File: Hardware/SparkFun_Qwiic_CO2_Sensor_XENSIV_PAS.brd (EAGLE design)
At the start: 25.4 x 40.6 mm, 72 parts, among them J1 QWIIC_RA, J2 QWIIC_RA, U1 PASCO2V01BUMA1, U2 LMR62421

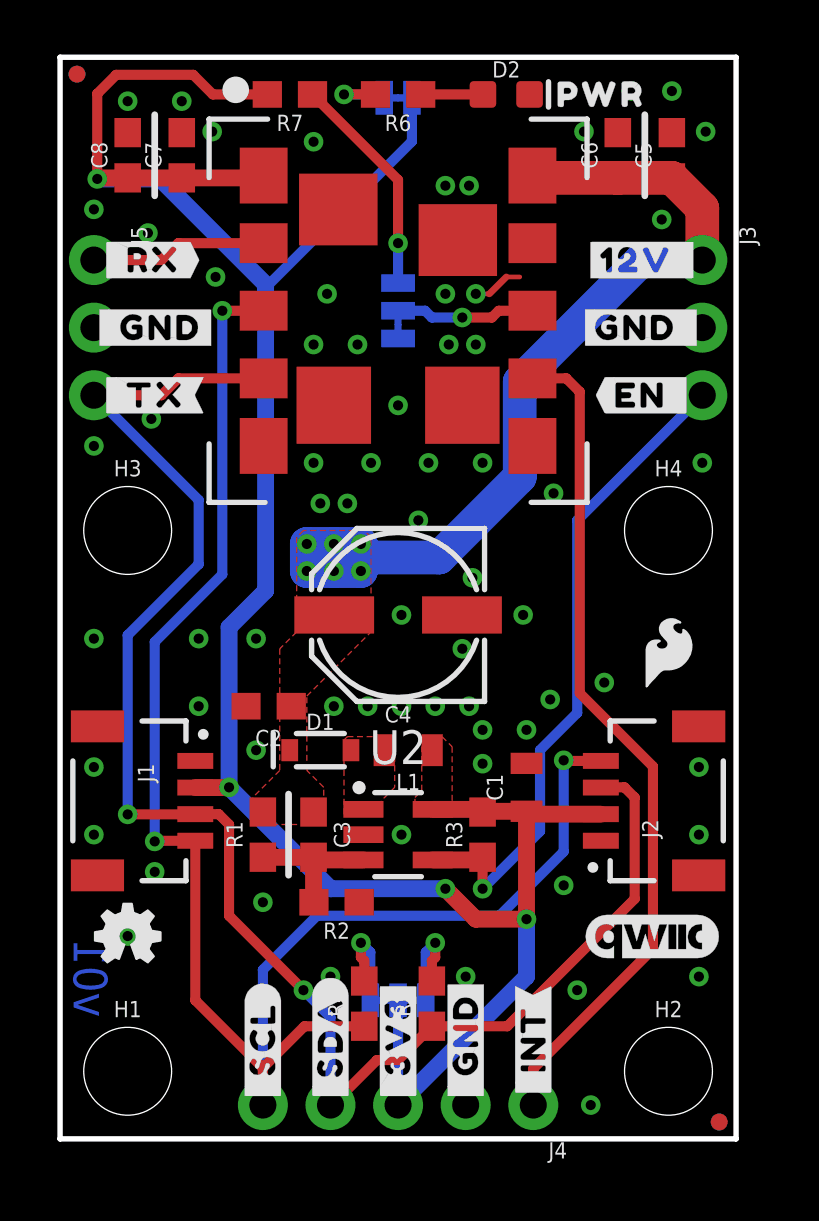
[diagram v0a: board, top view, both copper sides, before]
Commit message: Post design review changes and gerbers.
Add tDocu for the can and put squares for PnP.
Move EN to bottom row.
Rearrange I2C PTHs on bottom row to align with prior art.
Add PWM/PWM_DIS breakout.
Change silk on 12V to 12VIN.
Shift vertical PTHs down 0.05 to line up with perfboard holes.
Create gerbers.
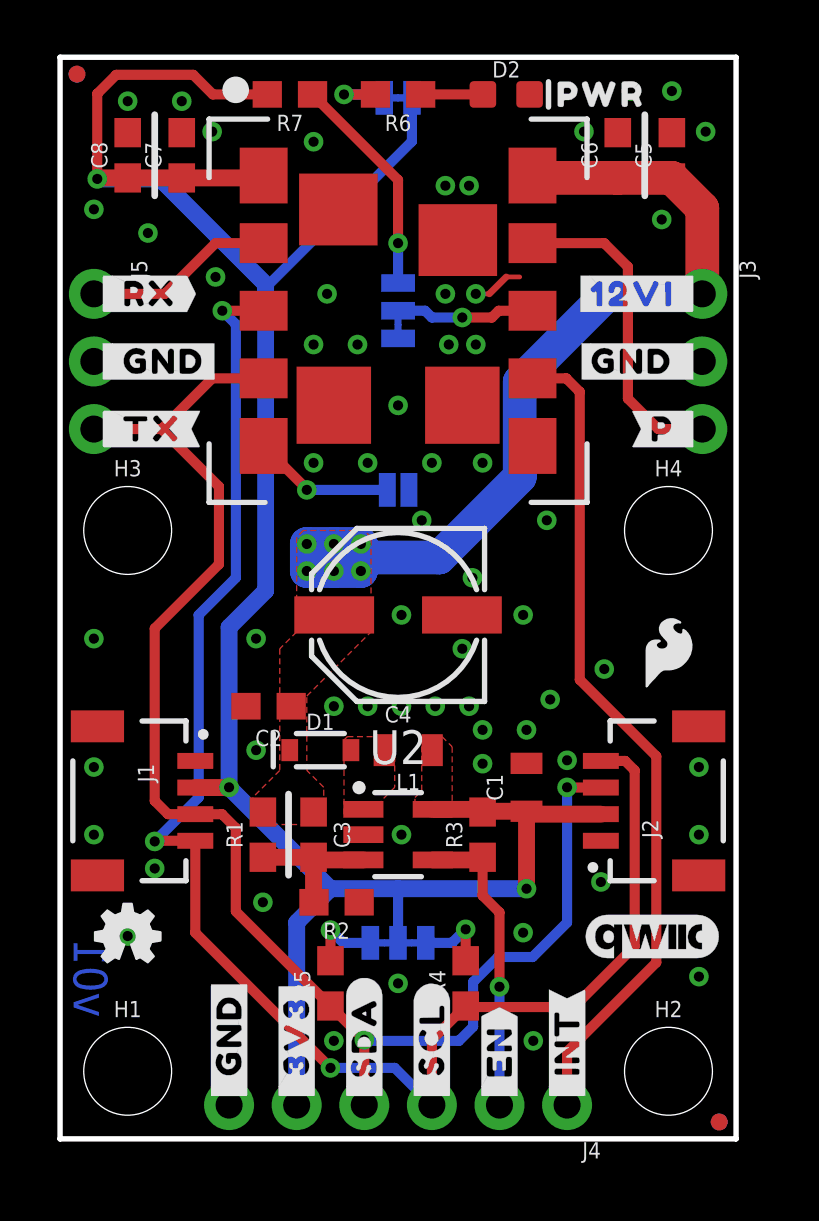
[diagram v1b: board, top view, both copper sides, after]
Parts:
- added PWM: JUMPER-SMT_2_NO_SILK, SparkFun-Jumpers:SMT-JUMPER_2_NO_SILK
- added U$33: (no value), output:#12VI_#0
- added U$34: (no value), output:#_PWM#0
- added U$35: (no value), output:#_SDA#0
- added U$36: (no value), output:#_SCL#0
- J4: device SparkFun-Connectors:1X05_NO_SILK -> SparkFun-Connectors:1X06_NO_SILK
- U$11: device output:#_12V#0 -> output:#_3V3#0
- U$16: device output:#_SDA#0 -> output:#PWM#0
- U$17: device output:#_SCL#0 -> output:#P_#0
- U$2: device output:#12V_#0 -> output:#_12VIN#0
- U$20: device output:#_SDA#TX#0 -> output:#_SDA#0
- U$3: device output:#EN_#0 -> output:#_EN#0
- moved U$11 33.5 mm to (8.89, 1.27), turned to 90 degrees
- moved U$17 30.3 mm to (24.1, 26.7), flipped to the top, turned to 0 degrees
- moved U$3 27.7 mm to (16.5, 1.27), turned to 90 degrees
- moved U$10 26.9 mm to (16.5, 1.27), turned to 90 degrees
- moved U$16 23.3 mm to (13.5, 24.4), flipped to the bottom, turned to 0 degrees
- moved U$14 8.89 mm to (6.35, 1.27)
- moved U$18 8.89 mm to (6.35, 1.27)
- moved U$15 6.35 mm to (14.0, 1.27)
- moved R4 3.89 mm to (15.2, 5.84)
- moved R5 3.89 mm to (10.2, 5.84)
- moved U$19 3.81 mm to (8.89, 1.27)
- moved I2C 2.16 mm to (12.7, 7.37), turned to 180 degrees
- moved U$27 2.16 mm to (12.7, 9.02)
- moved U$28 2.05 mm to (13.6, 39.1)
- moved U$12 1.28 mm to (1.27, 31.8)
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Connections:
- new net N$9: PWM.2, U1.5
- new net PWM_OUT: J3.3, U1.9
- net 3.3V: now also J4.5; no longer J4.3
- net EN: now also J4.2; no longer J3.3
- net GND: now also J4.6, PWM.1; no longer J4.2
- net SCL: now also J4.3; no longer J4.5
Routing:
- net EN: track 25.1 -> 11.5 mm
- net PWM_OUT: track 0.00 -> 12.2 mm
- net SDA/TX: track 61.1 -> 55.7 mm
- net N$9: track 0.00 -> 5.35 mm, vias 0 -> 1
- net 3.3V: track 91.2 -> 87.4 mm, vias 4 -> 3
- net SCL: track 62.6 -> 59.1 mm
- net N$1: track 3.79 -> 2.85 mm
- net N$3: track 3.79 -> 2.89 mm
- net 12V: track 35.7 -> 36.5 mm
- net RX: track 6.64 -> 7.17 mm
- net GND: vias 66 -> 60

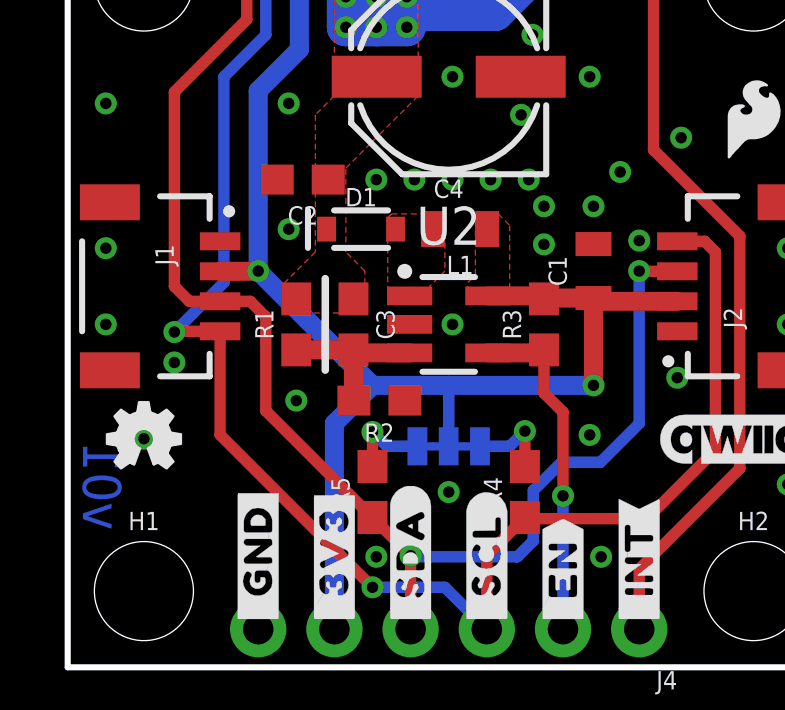
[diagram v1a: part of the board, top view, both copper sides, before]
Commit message: Update for v10.
Schematic - Make version v10.
Board - Make version v10. Change size of Silk title text.
Production - Removed individual board gerbers, add panel gerbers.
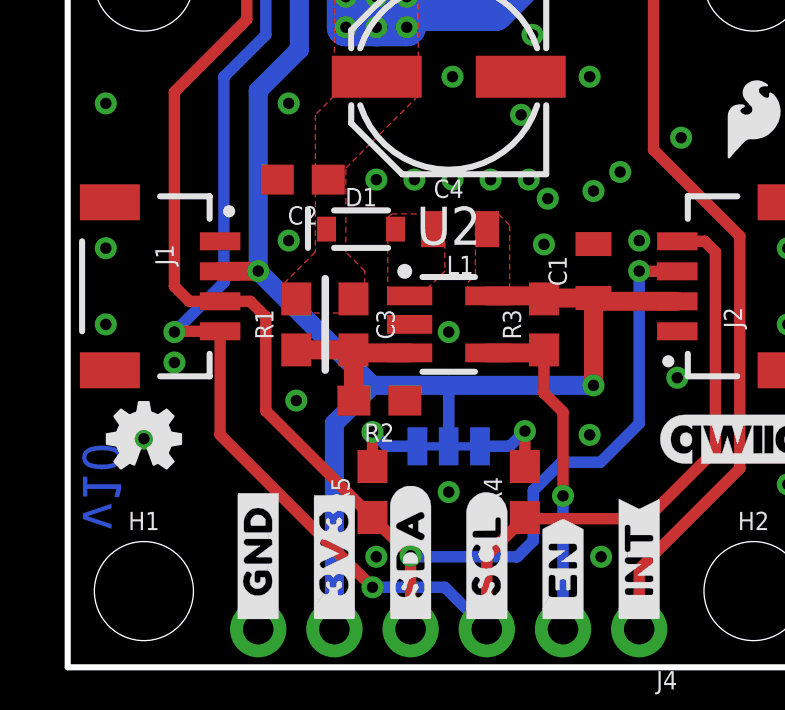
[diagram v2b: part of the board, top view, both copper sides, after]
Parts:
- removed U$23: (no value), output:CO2_SENSOR_#_PASCO2V010
- added U$37: (no value), output:PHOTOACOUSTIC0
- added U$38: (no value), output:SPECTROSCOPY0
- added U$39: (no value), output:PASCO2V010
- U$25: device output:PHOTOACOUSTIC_SPECTROSCOPY0 -> output:CO2_SENSOR0
- moved U$25 0.51 mm to (12.7, 11.9)
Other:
- board text added: "v10"
- board text removed: "v01"
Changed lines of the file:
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@@
 <drawing>
 <settings>
-<setting alwaysvectorfont="yes"/>
+<setting alwaysvectorfont="no"/>
 <setting verticaltext="up"/>
 </settings>
@@
 <layer number="27" name="tValues" color="7" fill="1" visible="no" active="yes"/>
 <layer number="28" name="bValues" color="7" fill="1" visible="no" active="yes"/>
-<layer number="29" name="tStop" color="7" fill="3" visible="yes" active="yes"/>
-<layer number="30" name="bStop" color="7" fill="6" visible="yes" active="yes"/>
-<layer number="31" name="tCream" color="7" fill="4" visible="yes" active="yes"/>
+<layer number="29" name="tStop" color="7" fill="3" visible="no" active="yes"/>
+<layer number="30" name="bStop" color="7" fill="6" visible="no" active="yes"/>
+<layer number="31" name="tCream" color="7" fill="4" visible="no" active="yes"/>
 <layer number="32" name="bCream" color="7" fill="5" visible="no" active="yes"/>
 <layer number="33" name="tFinish" color="6" fill="3" visible="no" active="yes"/>
@@
 <wire x1="8.5852" y1="12.954" x2="8.5852" y2="9.906" width="0.254" layer="21"/>
 <wire x1="3.556" y1="38.481" x2="3.556" y2="35.433" width="0.254" layer="21"/>
-<text x="0.508" y="4.572" size="1.27" layer="16" font="vector" ratio="15" rot="MR90">v01</text>
+<text x="0.508" y="4.572" size="1.27" layer="16" font="vector" ratio="15" rot="MR90">v10</text>
 <dimension x1="0" y1="0" x2="12.7" y2="31.115" x3="6.35" y3="-10.287" textsize="1.27" textratio="15" layer="47" dtype="horizontal" unit="inch"/>
 <dimension x1="0" y1="0" x2="22.86" y2="2.54" x3="11.43" y3="-13.081" textsize="1.27" textratio="15" layer="47" dtype="horizontal" unit="inch"/>
@@
 <element name="FRAME1" library="SparkFun-Aesthetics" package="CREATIVE_COMMONS" value="FRAME-LETTER" x="51.943" y="-9.398" smashed="yes">
 <attribute name="DESIGNER" value="Alex Brudner" x="51.943" y="-9.398" size="1.778" layer="27" display="off"/>
-<attribute name="REV" value="v01" x="51.943" y="-9.398" size="1.778" layer="27" display="off"/>
+<attribute name="REV" value="v10" x="51.943" y="-9.398" size="1.778" layer="27" display="off"/>
 </element>
 <element name="U1" library="xensiv_pas" package="LG-MLGA-14-1_Z8B00206105" value="PASCO2V01BUMA1" x="12.7" y="31.115" smashed="yes" rot="R270">
@@
 <element name="U2" library="xensiv_pas" package="SOT95P280X145-5M" package3d_urn="urn:adsk.eagle:package:40937508/1" value="LMR62421" x="12.7" y="11.43" smashed="yes">
 <attribute name="NAME" x="12.7" y="14.0836" size="1.27" layer="25" align="bottom-center"/>
-<attribute name="PROD_ID" value="IC-" x="12.7" y="11.43" size="1.778" layer="27" display="off"/>
+<attribute name="PROD_ID" value="VREG-19362" x="12.7" y="11.43" size="1.778" layer="27" display="off"/>
 <attribute name="VALUE" x="12.7" y="9.2164" size="1.27" layer="27" align="top-center"/>
 </element>
@@
 <element name="U$22" library="output" package="#_INT#0" value="" x="19.05" y="1.27" smashed="yes" rot="MR90"/>
 <element name="U$24" library="output" package="#PSEL#0" value="" x="11.049" y="28.702" smashed="yes" rot="MR90"/>
-<element name="U$25" library="output" package="PHOTOACOUSTIC_SPECTROSCOPY0" value="" x="12.7" y="12.446" smashed="yes" rot="MR0"/>
 <element name="U$27" library="output" package="#I�C#0" value="" x="12.7" y="9.017" smashed="yes" rot="MR0"/>
-<element name="U$23" library="output" package="CO2_SENSOR_#_PASCO2V010" value="" x="12.7" y="10.795" smashed="yes" rot="MR0"/>
 <element name="U$26" library="SparkFun-Aesthetics" package="SFE_LOGO_FLAME_STOP_.1" value="" x="22.86" y="36.83" smashed="yes" rot="MR0"/>
 <element name="R6" library="SparkFun-Resistors" package="0603" value="4.7k" x="12.7" y="39.243" smashed="yes" rot="R180">
@@
 <element name="U$35" library="output" package="#_SDA#0" value="" x="11.43" y="1.27" smashed="yes" rot="MR90"/>
 <element name="U$36" library="output" package="#_SCL#0" value="" x="13.97" y="1.27" smashed="yes" rot="MR90"/>
+<element name="U$37" library="output" package="PHOTOACOUSTIC0" value="" x="12.7" y="14.986" smashed="yes" rot="MR0"/>
+<element name="U$38" library="output" package="SPECTROSCOPY0" value="" x="12.7" y="13.462" smashed="yes" rot="MR0"/>
+<element name="U$25" library="output" package="CO2_SENSOR0" value="" x="12.7" y="11.938" smashed="yes" rot="MR0"/>
+<element name="U$39" library="output" package="PASCO2V010" value="" x="12.7" y="10.287" smashed="yes" rot="MR0"/>
 </elements>
 <signals>
@@
 </polygon>
 <via x="7.366" y="18.796" extent="1-16" drill="0.381"/>
-<via x="12.827" y="11.43" extent="1-16" drill="0.381"/>
+<via x="12.7" y="11.176" extent="1-16" drill="0.381"/>
 <via x="15.875" y="14.097" extent="1-16" drill="0.381"/>
 <via x="24.003" y="11.43" extent="1-16" drill="0.381"/>
@@
 <via x="15.494" y="21.082" extent="1-16" drill="0.381"/>
 <via x="15.113" y="18.415" extent="1-16" drill="0.381"/>
-<via x="17.526" y="15.367" extent="1-16" drill="0.381"/>
+<via x="17.526" y="15.875" extent="1-16" drill="0.381"/>
 <via x="11.557" y="16.256" extent="1-16" drill="0.381"/>
 <via x="12.827" y="16.256" extent="1-16" drill="0.381"/>
 <via x="14.097" y="16.256" extent="1-16" drill="0.381"/>
 <via x="15.367" y="16.256" extent="1-16" drill="0.381"/>
-<via x="15.875" y="15.367" extent="1-16" drill="0.381"/>
-<via x="7.366" y="14.605" extent="1-16" drill="0.381"/>
+<via x="16.002" y="15.621" extent="1-16" drill="0.381"/>
+<via x="7.366" y="14.224" extent="1-16" drill="0.381"/>
 <via x="20.447" y="17.653" extent="1-16" drill="0.381"/>
 <via x="18.415" y="16.51" extent="1-16" drill="0.381"/>

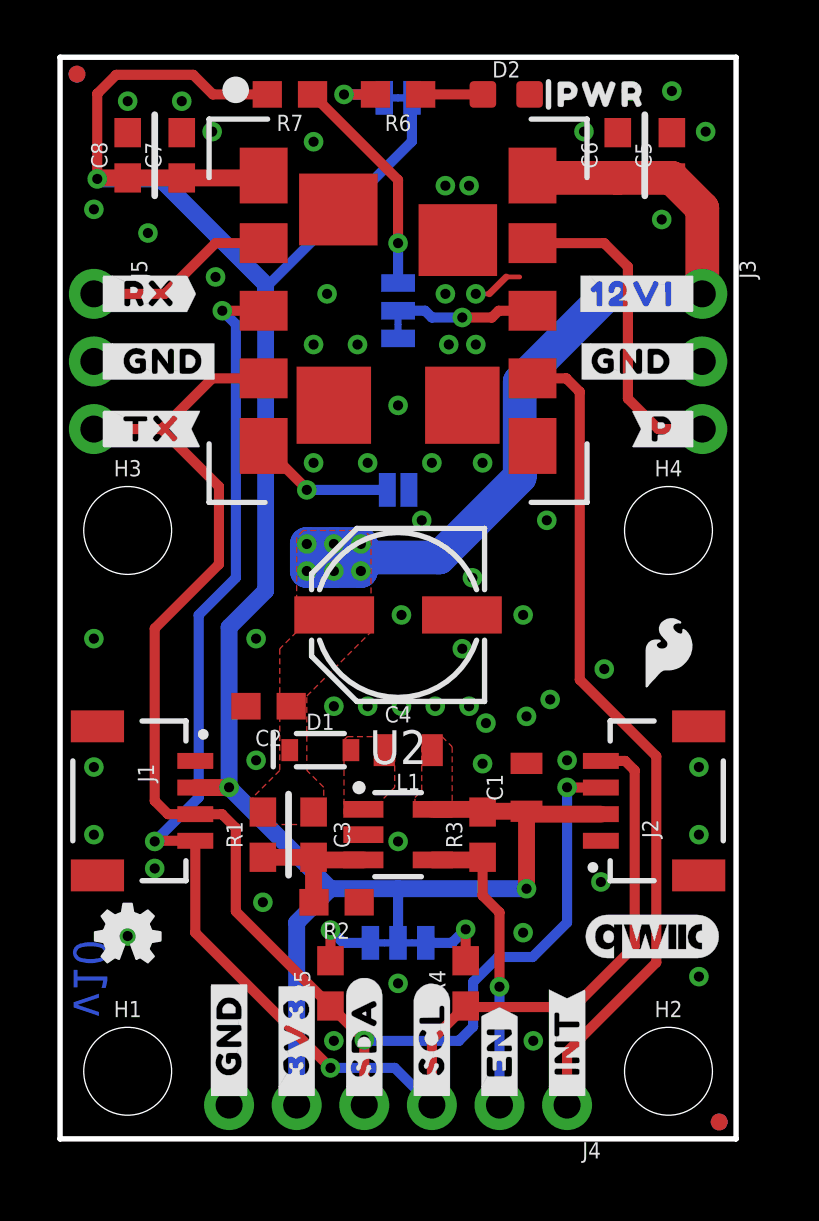
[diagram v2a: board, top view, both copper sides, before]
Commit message: Move Flame silk to middle.
Repanelize after.
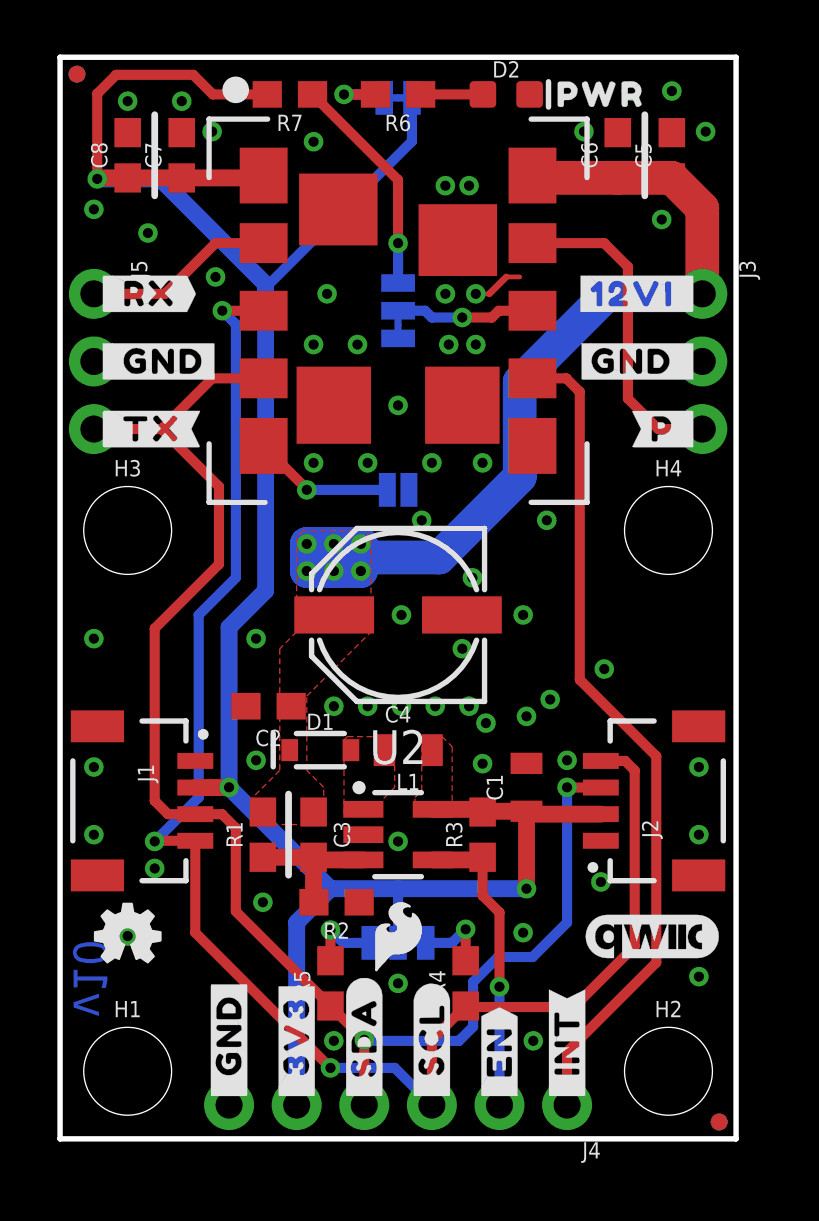
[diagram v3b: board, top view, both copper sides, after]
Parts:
- moved U$1 14.7 mm to (12.7, 7.62)
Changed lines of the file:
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@@
 <drawing>
 <settings>
-<setting alwaysvectorfont="no"/>
+<setting alwaysvectorfont="yes"/>
 <setting verticaltext="up"/>
 </settings>
@@
 <attribute name="VALUE" x="22.098" y="33.02" size="0.6096" layer="27" font="vector" ratio="20" rot="R270"/>
 </element>
-<element name="U$1" library="SparkFun-Aesthetics" package="SFE_LOGO_FLAME_.1" value="" x="22.86" y="18.288" smashed="yes"/>
+<element name="U$1" library="SparkFun-Aesthetics" package="SFE_LOGO_FLAME_.1" value="" x="12.7" y="7.62" smashed="yes"/>
 <element name="U$4" library="output" package="#GND_#0" value="" x="24.13" y="29.21" smashed="yes"/>
 <element name="U$5" library="output" package="#GND_#0" value="" x="1.27" y="29.21" smashed="yes" rot="MR0"/>
